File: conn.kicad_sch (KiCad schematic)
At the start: 74 parts, among them J10 MicroFit_2x04, J11 JST_S4B-XH, J12 MicroFit_2x04, J13 JST_B2B-XH, J14 JST_S2B-XH, J15 DNI, J16 MLX_1x03, J17 MLX_1x03, J5 JST_S6B-XH, J6 JST_S4B-XH, J7 MicroFit_2x04, J8 JST_S4B-XH, J9 JST_S4B-XH, SW2 DNI

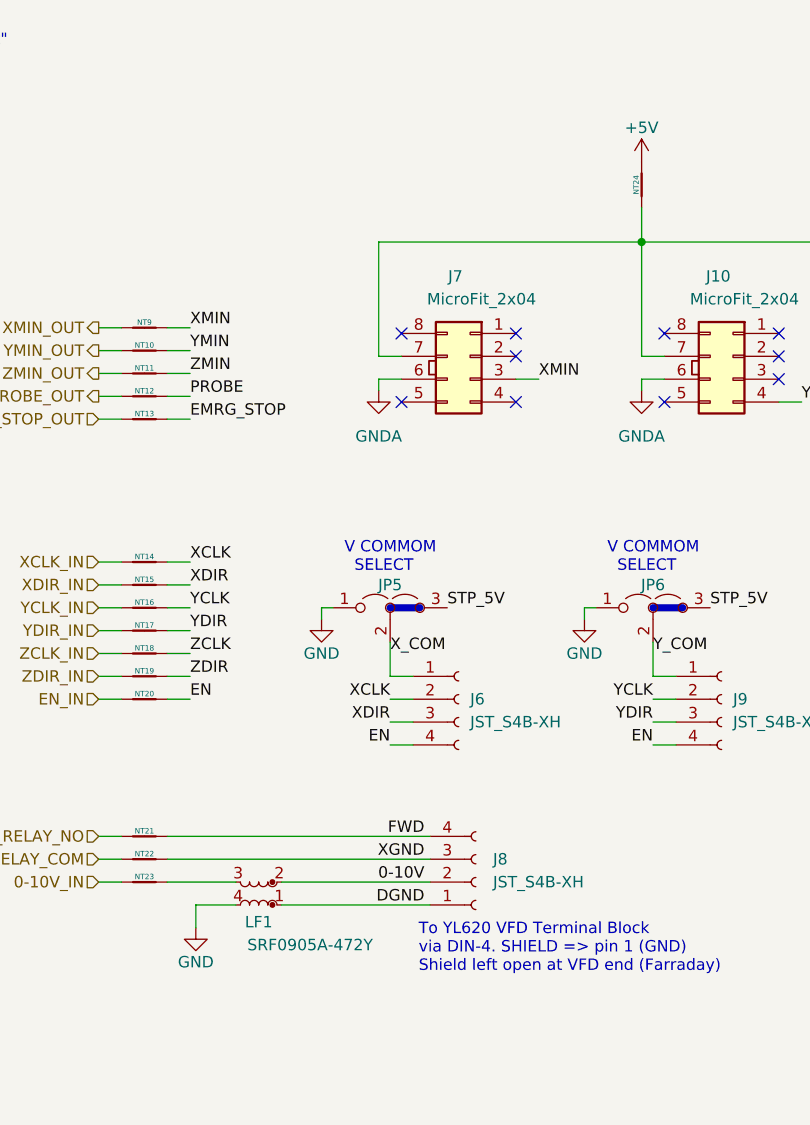
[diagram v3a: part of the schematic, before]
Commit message: Fixed yesterday's fix. Changed relay layout to allow 3A max terminal current, actually. Also changed VFD 0-10V PCB Farraday shield to reference VFD AGND instead of local GND.
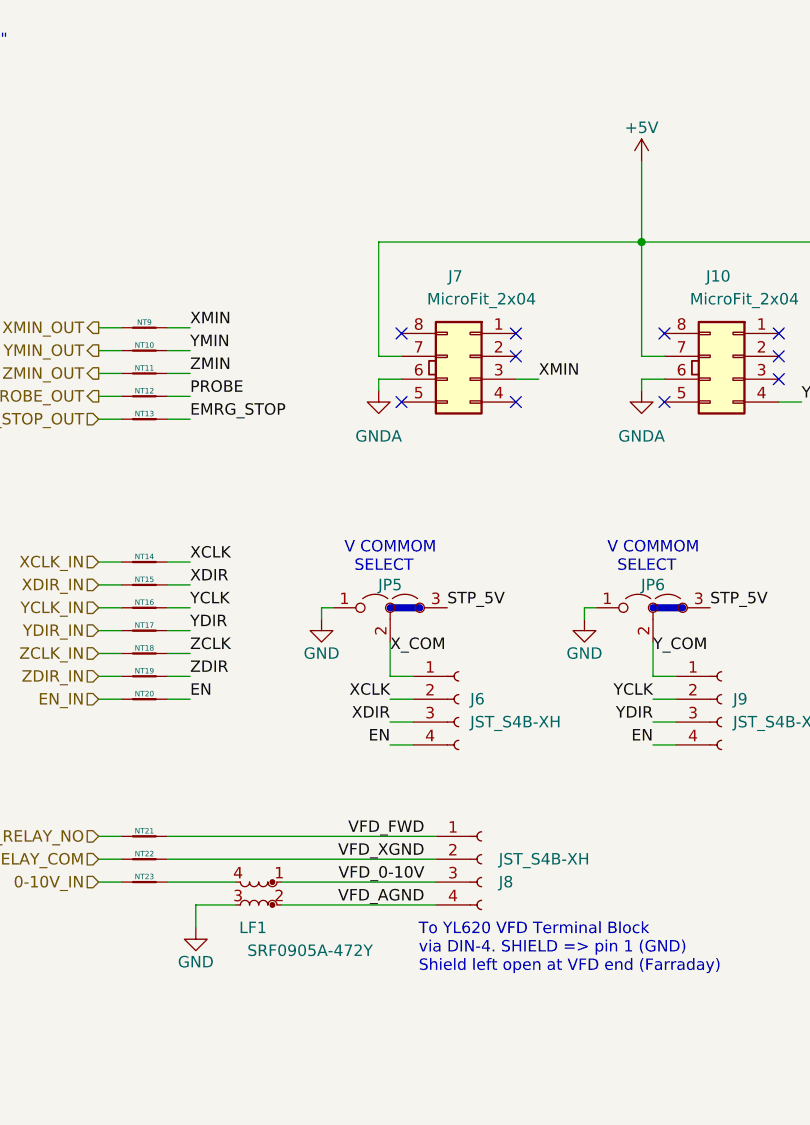
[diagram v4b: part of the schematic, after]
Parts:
- removed NT24: DNI, -Project:NetTie-2_SMD_Pad1.0mm, symbol 3rd-party:NT_2_TT
- NT21, NT22: footprint -Project:NetTie-2_SMD_Pad0.3mm -> -Project:NetTie-2_SMD_Pad1.0mm
- NT23: footprint -Project:NetTie-2_SMD_Pad0.3mm -> -Project:NetTie-2_SMD_Pad0.5mm
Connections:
- net +5V: now also J10.7 (Pin_7), J12.7 (Pin_7), J7.7 (Pin_7)
- net GND: now also LF1.3; no longer LF1.4
- net at NT23.2: now also LF1.4; no longer LF1.3
- net 0-10V renamed VFD_AGND
- net VFD_AGND: now also J8.4 (Pin_4); no longer J8.2 (Pin_2)
- net DGND renamed VFD_0-10V
- net VFD_0-10V: now also J8.3 (Pin_3); no longer J8.1 (Pin_1)
- net FWD renamed VFD_FWD
- net VFD_FWD: now also J8.1 (Pin_1); no longer J8.4 (Pin_4)
- net XGND renamed VFD_XGND
- net VFD_XGND: now also J8.2 (Pin_2); no longer J8.3 (Pin_3)
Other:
- moved on the sheet: J8, LF1
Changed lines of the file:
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@@
     (stroke (width 0) (type default) (color 0 0 0 0))
   )
-  (wire (pts (xy 64.135 110.49) (xy 93.345 110.49))
+  (wire (pts (xy 64.135 110.49) (xy 93.98 110.49))
     (stroke (width 0) (type default) (color 0 0 0 0))
   )
@@
     (stroke (width 0) (type default) (color 0 0 0 0))
   )
-  (wire (pts (xy 76.835 113.03) (xy 93.345 113.03))
+  (wire (pts (xy 76.835 113.03) (xy 93.98 113.03))
     (stroke (width 0) (type default) (color 0 0 0 0))
   )
@@
     (stroke (width 0) (type default) (color 0 0 0 0))
   )
-  (wire (pts (xy 64.135 107.95) (xy 93.345 107.95))
+  (wire (pts (xy 64.135 107.95) (xy 93.98 107.95))
     (stroke (width 0) (type default) (color 0 0 0 0))
   )
@@
     (stroke (width 0) (type default) (color 0 0 0 0))
   )
-  (wire (pts (xy 76.835 115.57) (xy 93.345 115.57))
+  (wire (pts (xy 76.835 115.57) (xy 93.98 115.57))
     (stroke (width 0) (type default) (color 0 0 0 0))
   )
@@
     (stroke (width 0) (type default) (color 0 0 0 0))
   )
-  (wire (pts (xy 116.84 38.1) (xy 116.84 41.91))
+  (wire (pts (xy 116.84 33.02) (xy 116.84 41.91))
     (stroke (width 0) (type default) (color 0 0 0 0))
   )
@@
     (effects (font (size 1.27 1.27)) (justify left bottom))
   )
-  (label "DGND" (at 92.71 115.57 180)
+  (label "VFD_AGND" (at 92.71 115.57 180)
     (effects (font (size 1.27 1.27)) (justify right bottom))
   )
@@
     (effects (font (size 1.27 1.27)) (justify right bottom))
   )
-  (label "XGND" (at 92.71 110.49 180)
+  (label "VFD_XGND" (at 92.71 110.49 180)
     (effects (font (size 1.27 1.27)) (justify right bottom))
   )
@@
     (effects (font (size 1.27 1.27)) (justify left bottom))
   )
-  (label "0-10V" (at 92.71 113.03 180)
+  (label "VFD_0-10V" (at 92.71 113.03 180)
     (effects (font (size 1.27 1.27)) (justify right bottom))
   )
@@
     (effects (font (size 1.27 1.27)) (justify right bottom))
   )
-  (label "FWD" (at 92.71 107.95 180)
+  (label "VFD_FWD" (at 92.71 107.95 180)
     (effects (font (size 1.27 1.27)) (justify right bottom))
   )
@@
     (pin "2")
   )
-  (symbol (lib_id "Connector:Conn_01x04_Female") (at 98.425 113.03 0) (mirror x) (unit 1)
-    (in_bom yes) (on_board yes)
-    (property "Reference" "J8" (id 0) (at 100.33 110.49 0)
+  (symbol (lib_id "Connector:Conn_01x04_Female") (at 99.06 110.49 0) (unit 1)
+    (in_bom yes) (on_board yes)
+    (property "Reference" "J8" (id 0) (at 100.965 113.03 0)
       (effects (font (size 1.27 1.27)) (justify left))
     )
-    (property "Value" "JST_S4B-XH" (id 1) (at 100.33 113.03 0)
+    (property "Value" "JST_S4B-XH" (id 1) (at 100.965 110.49 0)
       (effects (font (size 1.27 1.27)) (justify left))
     )
-    (property "Footprint" "Connector_JST:JST_EH_S4B-EH_1x04_P2.50mm_Horizontal" (id 2) (at 98.425 113.03 0)
-      (effects (font (size 1.27 1.27)) hide)
-    )
-    (property "Datasheet" "https://www.farnell.com/datasheets/2082976.pdf" (id 3) (at 98.425 113.03 0)
-      (effects (font (size 1.27 1.27)) hide)
-    )
-    (property "E14PART" "1516278" (id 5) (at 98.425 113.03 0)
-      (effects (font (size 1.27 1.27)) hide)
-    )
-    (property "JLCMFR#" "S4B-XH-A(LF)(SN)" (id 6) (at 98.425 113.03 0)
-      (effects (font (size 1.27 1.27)) hide)
-    )
-    (property "JLCPART" "C157925" (id 7) (at 98.425 113.03 0)
-      (effects (font (size 1.27 1.27)) hide)
-    )
-    (property "JLCMOQ" "2" (id 8) (at 98.425 113.03 0)
+    (property "Footprint" "Connector_JST:JST_EH_S4B-EH_1x04_P2.50mm_Horizontal" (id 2) (at 99.06 110.49 0)
+      (effects (font (size 1.27 1.27)) hide)
+    )
+    (property "Datasheet" "https://www.farnell.com/datasheets/2082976.pdf" (id 3) (at 99.06 110.49 0)
+      (effects (font (size 1.27 1.27)) hide)
+    )
+    (property "E14PART" "1516278" (id 5) (at 99.06 110.49 0)
+      (effects (font (size 1.27 1.27)) hide)
+    )
+    (property "JLCMFR#" "S4B-XH-A(LF)(SN)" (id 6) (at 99.06 110.49 0)
+      (effects (font (size 1.27 1.27)) hide)
+    )
+    (property "JLCPART" "C157925" (id 7) (at 99.06 110.49 0)
+      (effects (font (size 1.27 1.27)) hide)
+    )
+    (property "JLCMOQ" "2" (id 8) (at 99.06 110.49 0)
       (effects (font (size 1.27 1.27)) hide)
     )
@@
     (pin "6")
   )
-  (symbol (lib_id "Device:L_Coupled_Small_1423") (at 74.295 114.3 180) (unit 1)
-    (in_bom yes) (on_board yes)
-    (property "Reference" "LF1" (id 0) (at 74.295 117.475 0))
-    (property "Value" "SRF0905A-472Y" (id 1) (at 80.01 120.015 0))
+  (symbol (lib_id "Device:L_Coupled_Small_1423") (at 74.295 114.3 0) (mirror y) (unit 1)
+    (in_bom yes) (on_board yes)
+    (property "Reference" "LF1" (id 0) (at 73.66 118.11 0))
+    (property "Value" "SRF0905A-472Y" (id 1) (at 80.01 120.65 0))
     (property "Footprint" "Filter:Filter_Bourns_SRF0905_6.0x9.2mm" (id 2) (at 74.295 114.3 0)
       (effects (font (size 1.27 1.27)) hide)
@@
     (pin "2")
   )
-  (symbol (lib_id "3rd-party:NT_2_TT") (at 116.84 35.56 90) (unit 1)
-    (in_bom yes) (on_board yes)
-    (property "Reference" "NT24" (id 0) (at 116.24 35.56 0)
-      (effects (font (size 0.6 0.6)))
-    )
-    (property "Value" "DNI" (id 1) (at 114.3 35.56 0)
-      (effects (font (size 1.27 1.27)) hide)
-    )
-    (property "Footprint" "-Project:NetTie-2_SMD_Pad1.0mm" (id 2) (at 116.84 35.56 0)
-      (effects (font (size 1.27 1.27)) hide)
-    )
-    (property "Datasheet" "~" (id 3) (at 116.84 35.56 0)
-      (effects (font (size 1.27 1.27)) hide)
-    )
-    (pin "1")
-    (pin "2")
-  )
   (symbol (lib_id "3rd-party:NT_2_TT") (at 61.595 107.95 0) (unit 1)
     (in_bom yes) (on_board yes)
@@
       (effects (font (size 1.27 1.27)) hide)
     )
-    (property "Footprint" "-Project:NetTie-2_SMD_Pad0.3mm" (id 2) (at 61.595 107.95 0)
+    (property "Footprint" "-Project:NetTie-2_SMD_Pad1.0mm" (id 2) (at 61.595 107.95 0)
       (effects (font (size 1.27 1.27)) hide)
     )
@@
       (effects (font (size 1.27 1.27)) hide)
     )
-    (property "Footprint" "-Project:NetTie-2_SMD_Pad0.3mm" (id 2) (at 61.595 113.03 0)
+    (property "Footprint" "-Project:NetTie-2_SMD_Pad0.5mm" (id 2) (at 61.595 113.03 0)
       (effects (font (size 1.27 1.27)) hide)
     )
@@
       (effects (font (size 1.27 1.27)) hide)
     )
-    (property "Footprint" "-Project:NetTie-2_SMD_Pad0.3mm" (id 2) (at 61.595 110.49 0)
-      (effects (font (size 1.27 1.27)) hide)
-    )
+    (property "Footprint" "-Project:NetTie-2_SMD_Pad1.0mm" (id 2) (at 61.595 110.49 0)
+      (effects (font (size 1.27 1.27)) hide)
+    )

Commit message: Part supply references wip.
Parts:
- J10, J12, J7: E14MFR# (none) -> 43045-1027; E14PART 1654450 -> 1513893; JLCMFR# DNI -> Mouser
- NT10, NT11, NT12, NT13, NT14, NT15, NT16, NT17, NT18, NT19, NT20, NT21, NT22, NT23, NT25, NT26, NT27, NT4, NT5, NT6, NT7, NT8, NT9: E14MFR# (none) -> DNI; JLCMFR# (none) -> DNI
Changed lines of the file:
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@@
+      (effects (font (size 1.27 1.27)) hide)
+    )
+    (property "E14MFR#" "DNI" (id 4) (at 154.94 109.22 0)
+      (effects (font (size 1.27 1.27)) hide)
+    )
+    (property "JLCMFR#" "DNI" (id 5) (at 154.94 109.22 0)
       (effects (font (size 1.27 1.27)) hide)
     )
@@
       (effects (font (size 1.27 1.27)) hide)
     )
+    (property "E14MFR#" "DNI" (id 4) (at 50.8 172.72 0)
+      (effects (font (size 1.27 1.27)) hide)
+    )
+    (property "JLCMFR#" "DNI" (id 5) (at 50.8 172.72 0)
+      (effects (font (size 1.27 1.27)) hide)
+    )
     (pin "1")
     (pin "2")
@@
     )
     (property "Datasheet" "~" (id 3) (at 61.595 51.435 0)
+      (effects (font (size 1.27 1.27)) hide)
+    )
+    (property "E14MFR#" "DNI" (id 4) (at 61.595 51.435 0)
+      (effects (font (size 1.27 1.27)) hide)
+    )
+    (property "JLCMFR#" "DNI" (id 5) (at 61.595 51.435 0)
       (effects (font (size 1.27 1.27)) hide)
     )
@@
       (effects (font (size 1.27 1.27)) hide)
     )
+    (property "E14MFR#" "DNI" (id 4) (at 50.8 170.18 0)
+      (effects (font (size 1.27 1.27)) hide)
+    )
+    (property "JLCMFR#" "DNI" (id 5) (at 50.8 170.18 0)
+      (effects (font (size 1.27 1.27)) hide)
+    )
     (pin "1")
     (pin "2")
@@
     )
     (property "Datasheet" "~" (id 3) (at 167.64 80.01 0)
+      (effects (font (size 1.27 1.27)) hide)
+    )
+    (property "E14MFR#" "DNI" (id 4) (at 167.64 80.01 0)
+      (effects (font (size 1.27 1.27)) hide)
+    )
+    (property "JLCMFR#" "DNI" (id 5) (at 167.64 80.01 0)
       (effects (font (size 1.27 1.27)) hide)
     )
@@
       (effects (font (size 1.27 1.27)) hide)
     )
+    (property "E14MFR#" "DNI" (id 4) (at 61.595 77.47 0)
+      (effects (font (size 1.27 1.27)) hide)
+    )
+    (property "JLCMFR#" "DNI" (id 5) (at 61.595 77.47 0)
+      (effects (font (size 1.27 1.27)) hide)
+    )
     (pin "1")
     (pin "2")
@@
     )
     (property "Datasheet" "~" (id 3) (at 61.595 85.09 0)
+      (effects (font (size 1.27 1.27)) hide)
+    )
+    (property "E14MFR#" "DNI" (id 4) (at 61.595 85.09 0)
+      (effects (font (size 1.27 1.27)) hide)
+    )
+    (property "JLCMFR#" "DNI" (id 5) (at 61.595 85.09 0)
       (effects (font (size 1.27 1.27)) hide)
     )
@@
       (effects (font (size 1.27 1.27)) hide)
     )
+    (property "E14MFR#" "DNI" (id 4) (at 50.8 167.64 0)
+      (effects (font (size 1.27 1.27)) hide)
+    )
+    (property "JLCMFR#" "DNI" (id 5) (at 50.8 167.64 0)
+      (effects (font (size 1.27 1.27)) hide)
+    )
     (pin "1")
     (pin "2")
@@
       (effects (font (size 1.27 1.27)) hide)
     )
-    (property "E14PART" "1654450" (id 5) (at 157.48 54.61 0)
-      (effects (font (size 1.27 1.27)) hide)
-    )
-    (property "JLCMFR#" "DNI" (id 6) (at 157.48 54.61 0)
+    (property "E14PART" "1513893" (id 5) (at 157.48 54.61 0)
+      (effects (font (size 1.27 1.27)) hide)
+    )
+    (property "JLCMFR#" "Mouser" (id 6) (at 157.48 54.61 0)
+      (effects (font (size 1.27 1.27)) hide)
+    )
+    (property "E14MFR#" "43045-1027" (id 7) (at 157.48 54.61 0)
       (effects (font (size 1.27 1.27)) hide)
     )
@@
       (effects (font (size 1.27 1.27)) hide)
     )
+    (property "E14MFR#" "DNI" (id 4) (at 50.8 165.1 0)
+      (effects (font (size 1.27 1.27)) hide)
+    )
+    (property "JLCMFR#" "DNI" (id 5) (at 50.8 165.1 0)
+      (effects (font (size 1.27 1.27)) hide)
+    )
     (pin "1")
     (pin "2")
@@
     )
     (property "Datasheet" "~" (id 3) (at 61.595 92.71 0)
+      (effects (font (size 1.27 1.27)) hide)
+    )
+    (property "E14MFR#" "DNI" (id 4) (at 61.595 92.71 0)
+      (effects (font (size 1.27 1.27)) hide)
+    )
+    (property "JLCMFR#" "DNI" (id 5) (at 61.595 92.71 0)
       (effects (font (size 1.27 1.27)) hide)
     )
@@
       (effects (font (size 1.27 1.27)) hide)
     )
+    (property "E14MFR#" "DNI" (id 4) (at 60.96 153.67 0)
+      (effects (font (size 1.27 1.27)) hide)
+    )
+    (property "JLCMFR#" "DNI" (id 5) (at 60.96 153.67 0)
+      (effects (font (size 1.27 1.27)) hide)
+    )
     (pin "1")
     (pin "2")
@@
     )
     (property "Datasheet" "~" (id 3) (at 61.595 87.63 0)
+      (effects (font (size 1.27 1.27)) hide)
+    )
+    (property "E14MFR#" "DNI" (id 4) (at 61.595 87.63 0)
+      (effects (font (size 1.27 1.27)) hide)
+    )
+    (property "JLCMFR#" "DNI" (id 5) (at 61.595 87.63 0)
       (effects (font (size 1.27 1.27)) hide)
     )
@@
       (effects (font (size 1.27 1.27)) hide)
     )
+    (property "E14MFR#" "DNI" (id 4) (at 61.595 80.01 0)
+      (effects (font (size 1.27 1.27)) hide)
+    )
+    (property "JLCMFR#" "DNI" (id 5) (at 61.595 80.01 0)
+      (effects (font (size 1.27 1.27)) hide)
+    )
     (pin "1")
     (pin "2")
@@
       (effects (font (size 1.27 1.27)) hide)
     )
+    (property "E14MFR#" "DNI" (id 4) (at 61.595 90.17 0)
+      (effects (font (size 1.27 1.27)) hide)
+    )
+    (property "JLCMFR#" "DNI" (id 5) (at 61.595 90.17 0)
+      (effects (font (size 1.27 1.27)) hide)
+    )
     (pin "1")
     (pin "2")
@@
       (effects (font (size 1.27 1.27)) hide)
     )
+    (property "E14MFR#" "DNI" (id 4) (at 61.595 59.055 0)
+      (effects (font (size 1.27 1.27)) hide)
+    )
+    (property "JLCMFR#" "DNI" (id 5) (at 61.595 59.055 0)
+      (effects (font (size 1.27 1.27)) hide)
+    )
     (pin "1")
     (pin "2")
@@
       (effects (font (size 1.27 1.27)) hide)
     )
-    (property "E14PART" "1654450" (id 5) (at 127 54.61 0)
-      (effects (font (size 1.27 1.27)) hide)
-    )
-    (property "JLCMFR#" "DNI" (id 6) (at 127 54.61 0)
+    (property "E14PART" "1513893" (id 5) (at 127 54.61 0)
+      (effects (font (size 1.27 1.27)) hide)
+    )
+    (property "JLCMFR#" "Mouser" (id 6) (at 127 54.61 0)
+      (effects (font (size 1.27 1.27)) hide)
+    )
+    (property "E14MFR#" "43045-1027" (id 7) (at 127 54.61 0)
       (effects (font (size 1.27 1.27)) hide)
     )
@@
       (effects (font (size 1.27 1.27)) hide)
     )
+    (property "E14MFR#" "DNI" (id 4) (at 154.94 111.76 0)
+      (effects (font (size 1.27 1.27)) hide)
+    )
+    (property "JLCMFR#" "DNI" (id 5) (at 154.94 111.76 0)
+      (effects (font (size 1.27 1.27)) hide)
+    )
     (pin "1")
     (pin "2")
@@
       (effects (font (size 1.27 1.27)) hide)
     )
+    (property "E14MFR#" "DNI" (id 4) (at 61.595 53.975 0)
+      (effects (font (size 1.27 1.27)) hide)
+    )
+    (property "JLCMFR#" "DNI" (id 5) (at 61.595 53.975 0)
+      (effects (font (size 1.27 1.27)) hide)
+    )
     (pin "1")
     (pin "2")
@@
     )
     (property "Datasheet" "~" (id 3) (at 61.595 107.95 0)
+      (effects (font (size 1.27 1.27)) hide)
+    )
+    (property "E14MFR#" "DNI" (id 4) (at 61.595 107.95 0)
+      (effects (font (size 1.27 1.27)) hide)
+    )
+    (property "JLCMFR#" "DNI" (id 5) (at 61.595 107.95 0)
       (effects (font (size 1.27 1.27)) hide)
     )
@@
     )
     (property "Datasheet" "~" (id 3) (at 61.595 113.03 0)
+      (effects (font (size 1.27 1.27)) hide)
+    )
+    (property "E14MFR#" "DNI" (id 4) (at 61.595 113.03 0)
+      (effects (font (size 1.27 1.27)) hide)
+    )
+    (property "JLCMFR#" "DNI" (id 5) (at 61.595 113.03 0)
       (effects (font (size 1.27 1.27)) hide)
     )
@@
       (effects (font (size 1.27 1.27)) hide)
     )
+    (property "E14MFR#" "DNI" (id 4) (at 61.595 110.49 0)
+      (effects (font (size 1.27 1.27)) hide)
+    )
+    (property "JLCMFR#" "DNI" (id 5) (at 61.595 110.49 0)
+      (effects (font (size 1.27 1.27)) hide)
+    )
     (pin "1")
     (pin "2")
@@
       (effects (font (size 1.27 1.27)) hide)
     )
+    (property "E14MFR#" "DNI" (id 4) (at 61.595 56.515 0)
+      (effects (font (size 1.27 1.27)) hide)
+    )
+    (property "JLCMFR#" "DNI" (id 5) (at 61.595 56.515 0)
+      (effects (font (size 1.27 1.27)) hide)
+    )
     (pin "1")
     (pin "2")
@@
       (effects (font (size 1.27 1.27)) hide)
     )
+    (property "E14MFR#" "DNI" (id 4) (at 61.595 61.595 0)
+      (effects (font (size 1.27 1.27)) hide)
+    )
+    (property "JLCMFR#" "DNI" (id 5) (at 61.595 61.595 0)
+      (effects (font (size 1.27 1.27)) hide)
+    )
     (pin "1")
     (pin "2")
@@
     )
     (property "Datasheet" "~" (id 3) (at 61.595 82.55 0)
+      (effects (font (size 1.27 1.27)) hide)
+    )
+    (property "E14MFR#" "DNI" (id 4) (at 61.595 82.55 0)
+      (effects (font (size 1.27 1.27)) hide)
+    )
+    (property "JLCMFR#" "DNI" (id 5) (at 61.595 82.55 0)
       (effects (font (size 1.27 1.27)) hide)
     )
@@
       (effects (font (size 1.27 1.27)) hide)
     )
-    (property "E14PART" "1654450" (id 5) (at 97.79 54.61 0)
-      (effects (font (size 1.27 1.27)) hide)
-    )
-    (property "JLCMFR#" "DNI" (id 6) (at 97.79 54.61 0)
-      (effects (font (size 1.27 1.27)) hide)
-    )
+    (property "E14PART" "1513893" (id 5) (at 97.79 54.61 0)
+      (effects (font (size 1.27 1.27)) hide)
+    )
+    (property "JLCMFR#" "Mouser" (id 6) (at 97.79 54.61 0)
+      (effects (font (size 1.27 1.27)) hide)
+    )
+    (property "E14MFR#" "43045-1027" (id 7) (at 97.79 54.61 0)
+      (effects (font (size 1.27 1.27)) hide)
+    )

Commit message: WIP: Changing to terminal blocks for stepper, relay and VFD ports.
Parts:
- D12, D20, D28: JLCMFR# NCD0402G1 -> NCD0402R1; JLCPART C130723 -> C130719
- D14, D22, D30: JLCMFR# NCD0402O1 -> NCD0402R1; JLCPART C130720 -> C130719
- D15, D23, D31: JLCMFR# NCD0402O1 -> NCD0402G1; JLCPART C130720 -> C130723
- D16, D24, D26, D32: JLCMFR# NCD0402B1 -> NCD0402R1; JLCPART C130724 -> C130719
- D17, D25, D33: JLCMFR# NCD0402B1 -> NCD0402G1; JLCPART C130724 -> C130723
- D19, D27, D35: JLCMFR# NCD0402R1 -> NCD0402G1; JLCPART C130719 -> C130723
- J10, J12, J7: JLCMFR# Mouser -> Mouser:538-43045-1027
- J11, J6, J8, J9: E14MFR# (none) -> S4B-EH(LF)(SN); E14PART 1516278 -> 1830721
